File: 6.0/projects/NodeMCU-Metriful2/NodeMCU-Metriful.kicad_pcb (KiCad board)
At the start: 2 copper layers, 81.7 x 57.1 mm, 27 parts, among them CN1 RJ10, CN2 RJ10, CN3 RJ10, J1 GPIO, J4 Particle Sensor, Q1 BSS138BKW, Q2 NX2301P, U1 NodeMCU 1.0 (ESP-12E), U2 Metriful, U3 DS18B20

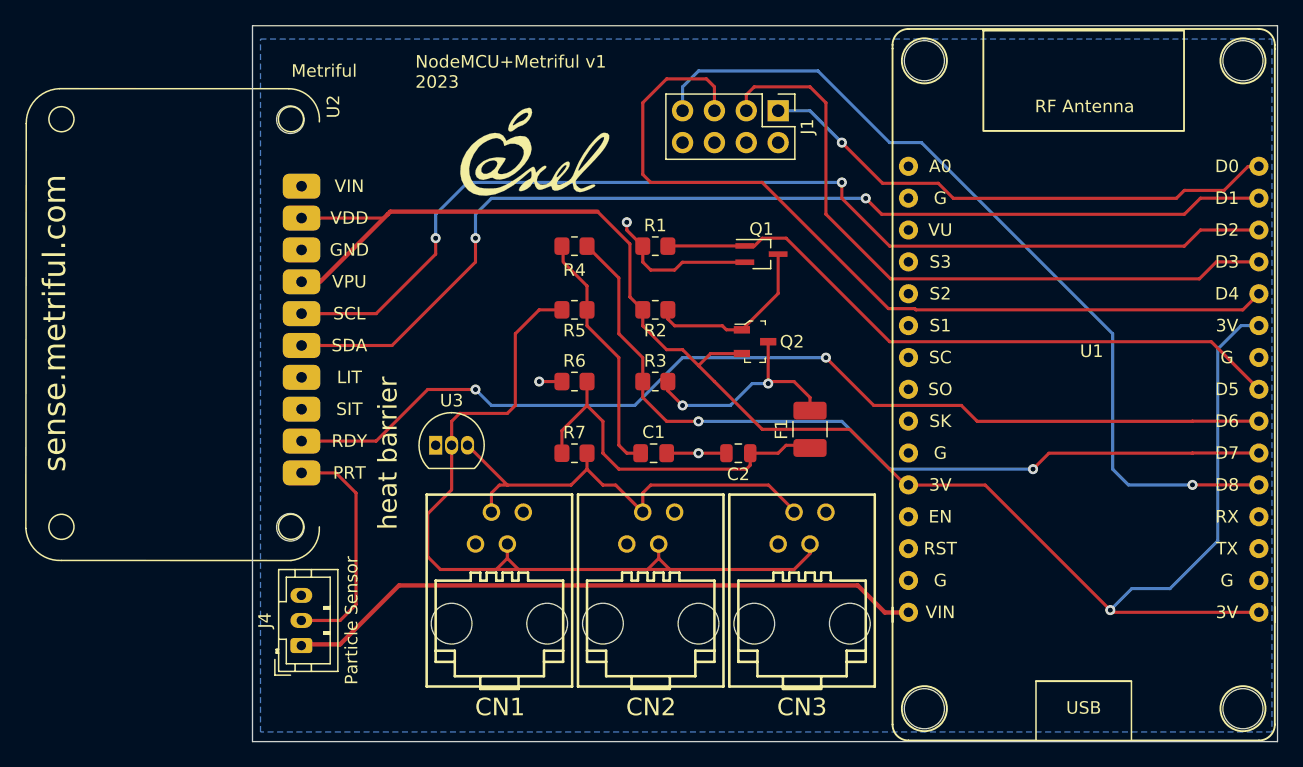
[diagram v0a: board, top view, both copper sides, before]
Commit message: Add header, move components to the left to make room for deep-sleep pin header
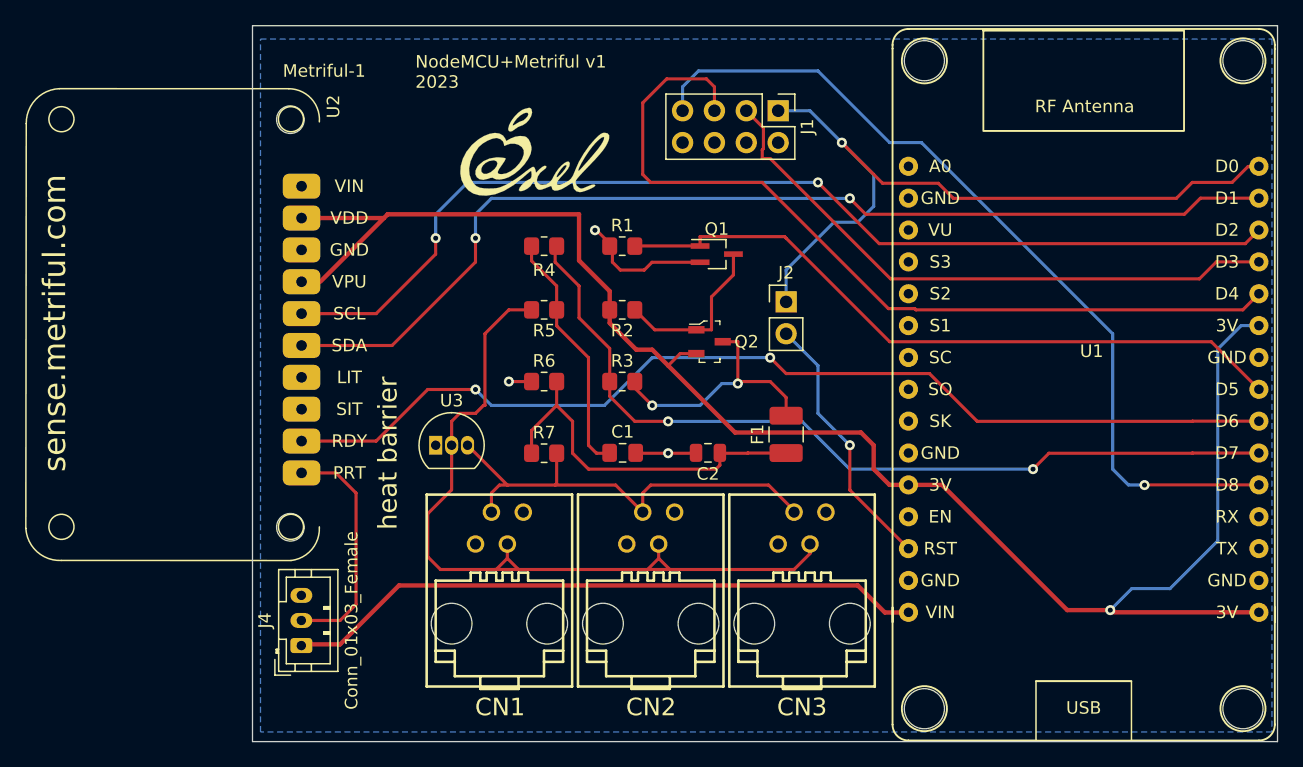
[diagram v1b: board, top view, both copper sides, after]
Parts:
- added J2: Deep Sleep, Connector_PinHeader_2.54mm:PinHeader_1x02_P2.54mm_Vertical, F.Cu at (132.7, 83.8)
- J1: value GPIO -> Conn_02x04_Odd_Even
- J4: value Particle Sensor -> Conn_01x03_Female
- U1: value NodeMCU 1.0 (ESP-12E) -> NodeMCU_1.0_(ESP-12E)
- U2: value Metriful -> Metriful-1
- moved Q2 3.63 mm to (126.6, 87.0)
- moved Q1 3.56 mm to (127.2, 80.0)
- moved R1 2.63 mm to (119.7, 79.4)
- moved R2 2.63 mm to (119.7, 84.5)
- moved R3 2.63 mm to (119.7, 90.2)
- moved C1 2.47 mm to (119.7, 95.9)
- moved C2 2.42 mm to (126.5, 95.9)
- moved R4 2.42 mm to (113.4, 79.4)
- moved R5 2.42 mm to (113.4, 84.5)
- moved R6 2.42 mm to (113.4, 90.2)
- moved R7 2.42 mm to (113.4, 95.9)
- moved F1 1.95 mm to (132.7, 94.4)
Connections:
- U1 pad 13: unconnected-(U1-Pad13) -> Net-(U1-Pad13)
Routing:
- net Net-(U1-Pad13): track 0.00 -> 21.2 mm, vias 0 -> 1
- net Net-(J1-Pad1): track 42.3 -> 60.0 mm
- net Net-(J1-Pad3): track 54.5 -> 48.5 mm
- net T_enable: track 52.4 -> 55.5 mm
- net Net-(R3-Pad1): track 65.9 -> 68.5 mm
- net Net-(CN1-Pad3): track 67.0 -> 64.6 mm
- net Net-(F1-Pad2): track 18.3 -> 20.5 mm
- net GND: track 18.9 -> 17.3 mm
- net +3V3: track 136.0 -> 134.7 mm
- net Net-(U1-Pad28): track 85.9 -> 85.0 mm
- net Net-(Q1-Pad3): track 14.2 -> 13.6 mm

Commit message: Many last-minute changes, mostly to silkscreen and some positioning
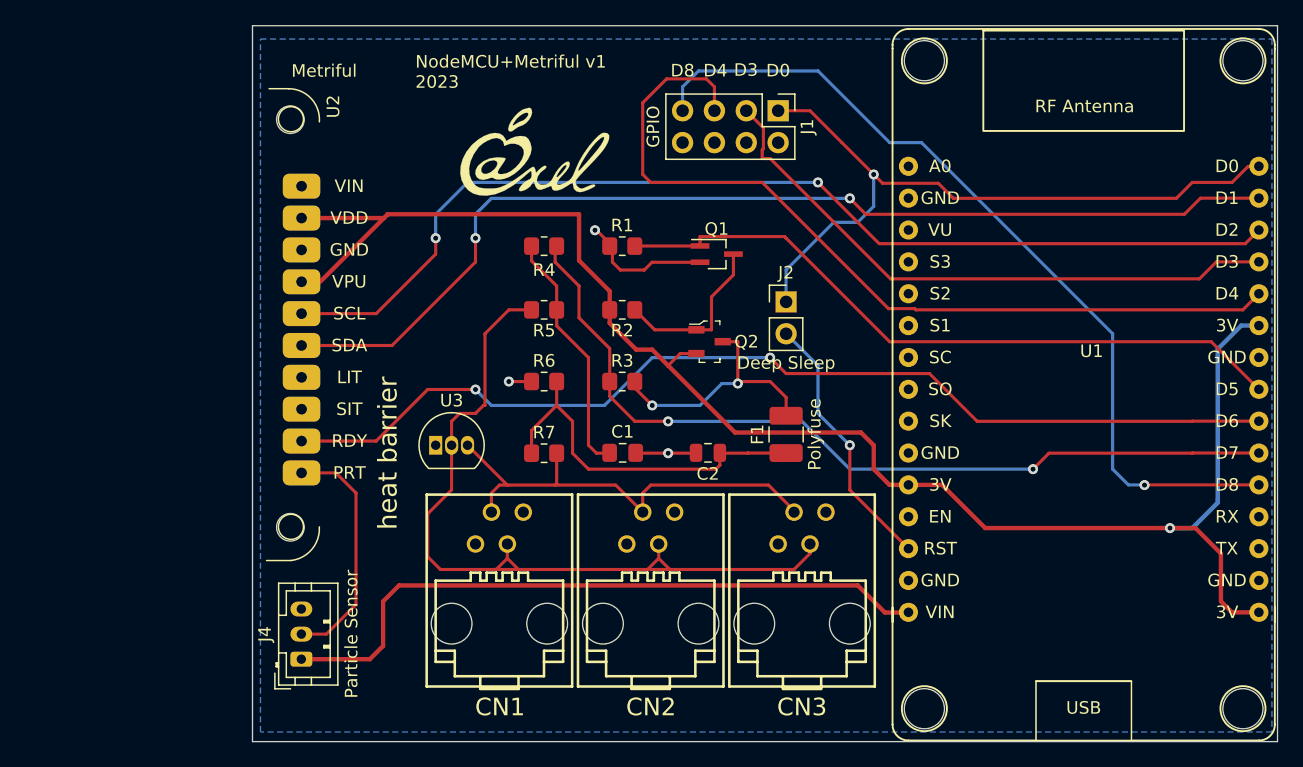
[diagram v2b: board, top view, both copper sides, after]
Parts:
- J1: value Conn_02x04_Odd_Even -> GPIO
- J4: value Conn_01x03_Female -> Particle Sensor
- U1: value NodeMCU_1.0_(ESP-12E) -> NodeMCU 1.0 (ESP-12E)
- U2: value Metriful-1 -> Metriful
- moved J4 1.09 mm to (94.1, 112.3)
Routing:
- net +3V3: track 134.7 -> 127.4 mm
- net Net-(J1-Pad1): track 60.0 -> 56.4 mm
- net VDD: track 51.1 -> 53.6 mm
